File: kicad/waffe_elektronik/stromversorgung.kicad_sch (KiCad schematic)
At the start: 27 parts, among them Q3 FS8205A, U1 MT3608, U15 DW01A, U2 AMS1117-3.3, U3 MCP73831

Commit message: Platine: günstigere JLC-Teile, Option ESP32-S3-WROOM-1U mit externer Antenne
- Flash ZD35Q1GC-IB, Kondensatoren/Dioden/Widerstände auf Basic-Teile und 0402, Layout angepasst
- WROOM-1U auf demselben Footprint: eigene JLCPCB-BOM/CPL (Modulmitte 3,15 mm versetzt),
  Mouser-Option mit Pigtail RP-SMA/U.FL und Knick-Stabantenne, 3D-Modell des 1U
- Gerber, BOM, CPL, Renders und Bestelllisten neu erzeugt

Co-Authored-By: Claude Opus 5.5 <noreply@anthropic.com>
Claude-Session: https://claude.ai/code/session_01KkZzubjLKyW9odUwvmxTog
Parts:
- BT1: LCSC C225233 -> (none)
- C1: LCSC C723734 -> C23742
- C3: footprint Capacitor_Tantalum_SMD:CP_EIA-3528-21_Kemet-B -> Capacitor_Tantalum_SMD:CP_EIA-3216-18_Kemet-A; LCSC C7193 -> C7171
- D4: value SS14 -> B5819W; footprint Diode_SMD:D_SOD-123F -> Diode_SMD:D_SOD-123; LCSC C2909920 -> C8598
- D5: value BAT54WS -> 1N5819WS; LCSC C168799 -> C191023

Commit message: Fertigung: JLCPCB-BOM/CPL mit allen Steckern und Tastern (Variante komplett)
- Handlötteile tragen im Schaltplan das Feld "LCSC Hand" statt "LCSC", build_board.py übernimmt es
- jlc_fab.py schreibt zusätzlich *_komplett und *_komplett_externe_antenne (79 Teile, 20 Extended),
  --check prüft den Bedarf der Komplett-Variante; Rotationskorrektur 180° für JST-SH (ungeprüft)
- Schaltplan und Platine neu erzeugt (Geometrie unverändert), Gerber neu, Doku angepasst

Co-Authored-By: Claude Opus 5.5 <noreply@anthropic.com>
Claude-Session: https://claude.ai/code/session_01KkZzubjLKyW9odUwvmxTog
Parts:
- BT1: LCSC Hand (none) -> C225233

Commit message: Platine: microSD-Slot gedreht, Ein/Aus über den Drehgeber-Taster, R7 12 Ω, 10 µF am Slot
- J7: Karte wird auf der Kontaktseite eingesteckt (Datenblatt TF-018) -> Slot gedreht, Kontakte und
  Öffnung an der Unterkante, SD-Leitungen neu verlegt
- Soft-Power: Q4 (AO3401A) trennt den Akku von BAT_SW, Taster an J5.2 schaltet über D6 (BAT54CW) ein,
  IO21 hält über Q5, IO9 liest den Taster; Lasche oben links 18,6 x 9 mm mit den neuen Teilen,
  Leitungen auf B.Cu über die Oberkante, Akku-Plus über In2
- R7 12 Ω (C17913), C28 10 µF an der microSD-Versorgung
- Gerber, BOM/CPL (alle Varianten), Mouser-BOM, Renders und Doku neu

Co-Authored-By: Claude Opus 5.5 <noreply@anthropic.com>
Claude-Session: https://claude.ai/code/session_01KkZzubjLKyW9odUwvmxTog
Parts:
- added D6: BAT54CW, Package_TO_SOT_SMD:SOT-323_SC-70, symbol Diode:BAT54CW
- added Q4: AO3401A, Package_TO_SOT_SMD:SOT-23, symbol Transistor_FET:AO3401A
- added Q5: AO3400A, Package_TO_SOT_SMD:SOT-23, symbol Transistor_FET:AO3400A
- added R38, R40: 100k, Resistor_SMD:R_0603_1608Metric, symbol Device:R
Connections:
- net BAT_P: now also Q4.2 (S), R38.2; no longer C19.1, C5.1, L1.1, R3.1, U1.4 (EN), U1.5 (IN), U3.3 (V_{BAT})
- net GND: now also Q5.2 (S), R40.2
- new net: D6.1, Q4.1 (G), Q5.3 (D), R38.1
- new net BAT_SW: C19.1, C5.1, L1.1, Q4.3 (D), R3.1, U1.4 (EN), U1.5 (IN), U3.3 (V_{BAT})
- new net ENC_SW: D6.2
- new net PWR_HOLD: Q5.1 (G), R40.1
- new net PWR_KEY: D6.3
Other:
- note added: "Ein/Aus (Taster am Drehgeber)"
- note added: "Ein: Taster am Drehgeber drücken, ESP32 hält über IO21. Aus: IO21 low."
- note added: "Mit USB setzt die Firmware IO21 high: Laden über Q4."

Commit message: Platine: IP5306 (2 A Laden + 5 V) statt MT3608/MCP73831, Ein/Aus über KEY, eigener I²C-Bus
Co-Authored-By: Claude Opus 5.5 <noreply@anthropic.com>
Claude-Session: https://claude.ai/code/session_01KkZzubjLKyW9odUwvmxTog
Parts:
- removed D3: SS34, Diode_SMD:D_SMA, symbol Diode:SS34
- removed D5: 1N5819WS, Diode_SMD:D_SOD-323, symbol Device:D_Schottky
- removed Q4: AO3401A, Package_TO_SOT_SMD:SOT-23, symbol Transistor_FET:AO3401A
- removed Q5: AO3400A, Package_TO_SOT_SMD:SOT-23, symbol Transistor_FET:AO3400A
- removed R25: 10k, Resistor_SMD:R_0603_1608Metric, symbol Device:R
- removed U1: MT3608, Package_TO_SOT_SMD:SOT-23-6, symbol Regulator_Switching:MT3608
- removed U3: MCP73831, Package_TO_SOT_SMD:SOT-23-5, symbol Battery_Management:MCP73831-2-OT
- added C29: 10u, Capacitor_SMD:C_0603_1608Metric, symbol Device:C
- added C30: 22u, Capacitor_SMD:C_0805_2012Metric, symbol Device:C
- added U1: IP5306-I2C, Package_SO:HSOP-8-1EP_3.9x4.9mm_P1.27mm_EP2.3x2.3mm_ThermalVias, symbol lasertag:IP5306
- C4: value 1u -> 10u; footprint Capacitor_SMD:C_0603_1608Metric -> Capacitor_SMD:C_0805_2012Metric; LCSC C15849 -> C15850
- C5: value 1u -> 22u; LCSC C15849 -> C59461
- L1: value 10u -> 1u; LCSC C408412 -> C408355
- R1: value 2k -> 2; LCSC C22975 -> C22977
- R2: value 10k -> 1; LCSC C25804 -> C22936
- R24: value 75k -> 10k; LCSC C23242 -> C25804
- R3, R4: value 100k -> 1M; LCSC C25803 -> C22935
- R38, R40: value 100k -> 4.7k; footprint Resistor_SMD:R_0603_1608Metric -> Resistor_SMD:R_0402_1005Metric; LCSC C25803 -> C25900
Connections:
- net CHRG_STAT is gone; now on net BAT_P: R2.2
- net PWR_HOLD is gone; now on net 3V3_MCU: R40.1
- net 3V3_MCU: now also R38.1; no longer R2.1
- net 5V_PERIPH: now also C30.1, U1.8 (VOUT); no longer R24.1
- net BAT_P: now also C19.1, L1.2, R3.1; no longer R38.2
- net GND: now also C29.2, C30.2, U1.9 (GND); no longer R1.2, R40.2
- net VBUS_NATIVE: now also R1.1, U1.1 (VIN)
- net at D6.1: now also R24.2; no longer R38.1
- removed net BAT_SW: C19.1, C5.1, L1.1, R3.1
- new net: C29.1, R1.2
- new net: C5.1, R2.1, U1.6 (BAT)
- new net: L1.1, U1.7 (SW)
- new net IP_KEY: R24.1, U1.5 (KEY)
- new net IP_SCL: R40.2, U1.2 (SCL)
- new net IP_SDA: R38.2, U1.3 (SDA)
- no-connect marks 1 -> 2
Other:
- note added: "Akku + Ein/Aus (Taster am Drehgeber)"
- note added: "Ein: Taster am Drehgeber kurz drücken. Aus: 2 s drücken oder per I²C (Firmware)."
- note added: "Laden + 5 V (IP5306) + 3,3 V"
- note added: "Laden 2 A (USB-C), 5 V Boost, Ein/Aus-Taste; Register per I²C (Firmware)"
- note removed: "Ein/Aus (Taster am Drehgeber)"
- note removed: "Ein: Taster am Drehgeber drücken, ESP32 hält über IO21. Aus: IO21 low."
- note removed: "Laden (USB-C)"
- note removed: "Mit USB setzt die Firmware IO21 high: Laden über Q4."
- note removed: "Stromversorgung"

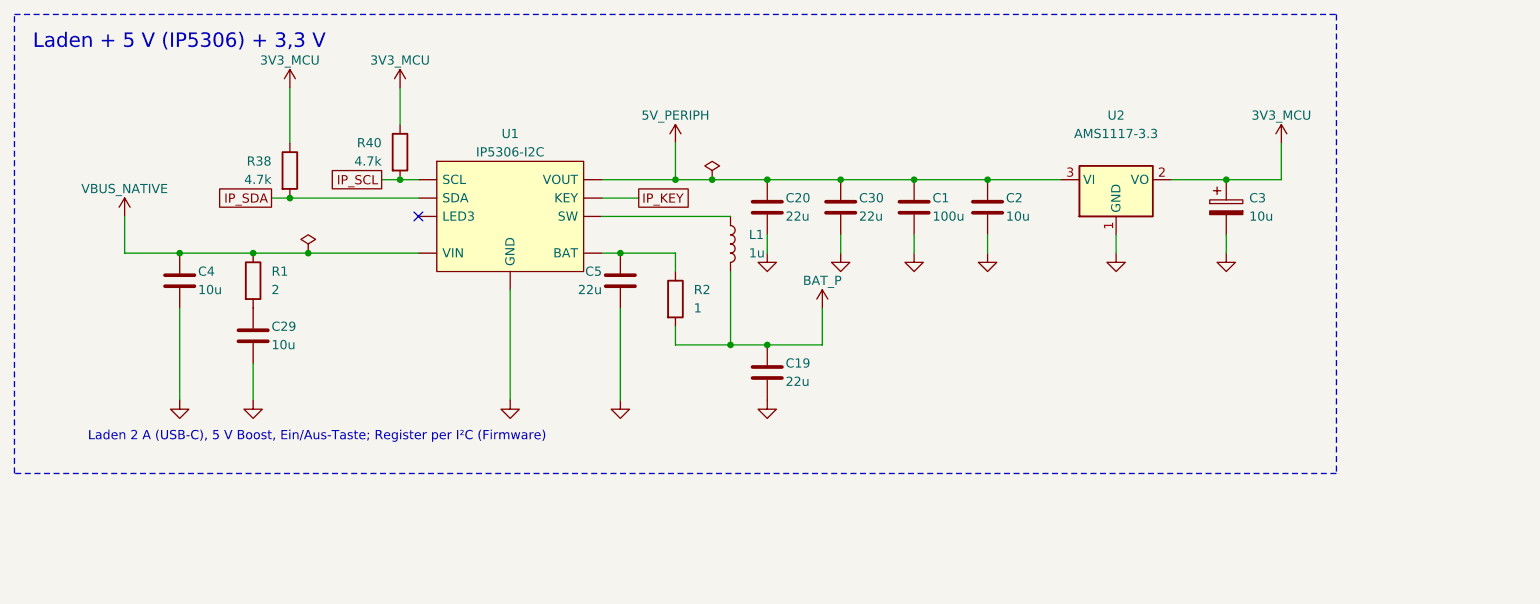
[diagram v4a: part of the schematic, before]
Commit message: Platine: Stecker zusammengelegt, Basic-Teile, MOSFET-Pegelwandler, Flash optional, Kabel-3V3 über 10 Ω, breitere 5-V- und Akku-Wege
Co-Authored-By: Claude Opus 5.5 <noreply@anthropic.com>
Claude-Session: https://claude.ai/code/session_01KkZzubjLKyW9odUwvmxTog
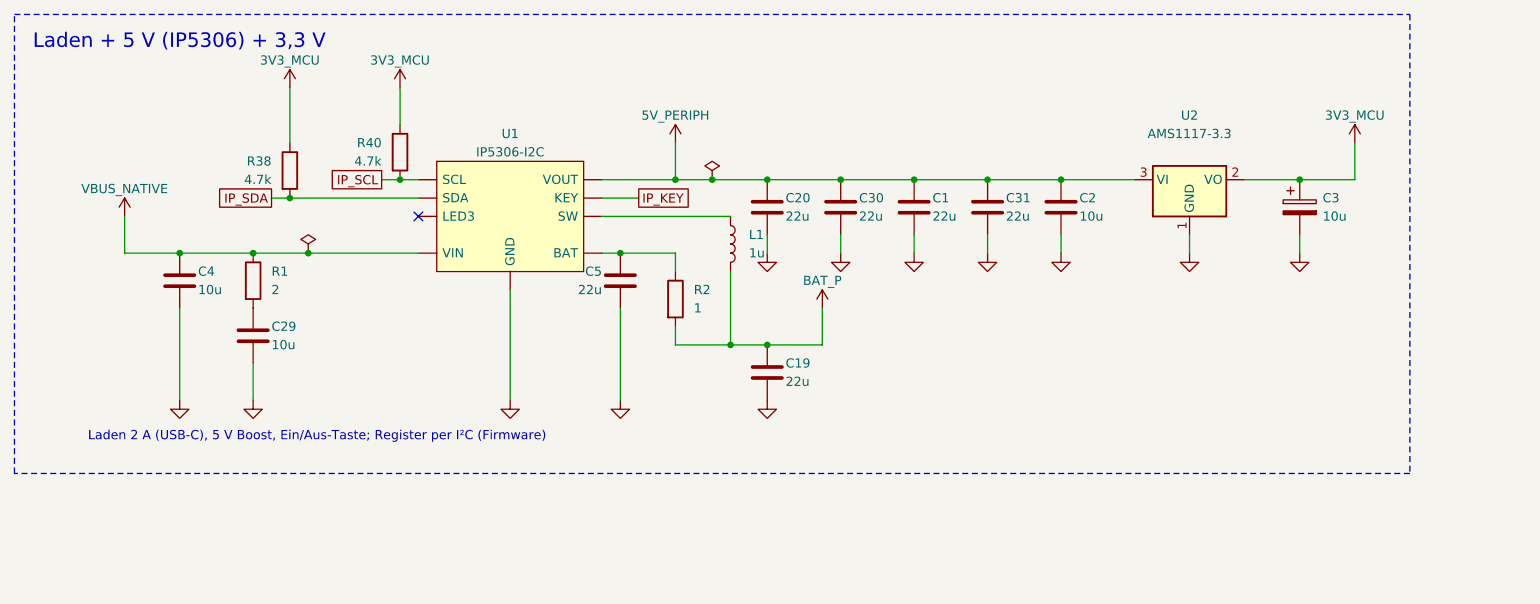
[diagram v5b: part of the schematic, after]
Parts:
- added C31: 22u, Capacitor_SMD:C_0805_2012Metric, symbol Device:C
- C1: value 100u -> 22u; footprint Capacitor_SMD:C_1210_3225Metric -> Capacitor_SMD:C_0805_2012Metric; LCSC C23742 -> C45783
- D6: LCSC C83573 -> C57891
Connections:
- net 5V_PERIPH: now also C31.1
- net GND: now also C31.2

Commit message: Platine: Lastschalter TPS22810 hinter dem IP5306 (EN = IRQ), RESET in die Lasche, Dämpfung an der USB-Buchse
Co-Authored-By: Claude Opus 5.5 <noreply@anthropic.com>
Claude-Session: https://claude.ai/code/session_01KkZzubjLKyW9odUwvmxTog
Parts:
- added C33: 10n, Capacitor_SMD:C_0402_1005Metric, symbol Device:C
- added R42: 100k, Resistor_SMD:R_0603_1608Metric, symbol Device:R
- added U16: TPS22810, Package_TO_SOT_SMD:SOT-23-6, symbol Power_Management:TPS22810DBV
- C30: value 22u -> 10u; footprint Capacitor_SMD:C_0805_2012Metric -> Capacitor_SMD:C_0603_1608Metric; LCSC C45783 -> C19702
- C4: footprint Capacitor_SMD:C_0805_2012Metric -> Capacitor_SMD:C_0603_1608Metric; LCSC C15850 -> C19702
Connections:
- net 5V_PERIPH: now also U16.6 (VOUT); no longer C20.1, C30.1, U1.8 (VOUT)
- net GND: now also C33.2, R42.2, U16.2 (GND)
- net IP_IRQ: now reaches U1.4 (IRQ)
- net IP_IRQ: now also R42.1, U16.3 (EN/UVLO)
- new net: C20.1, C30.1, U1.8 (VOUT), U16.1 (VIN)
- new net: C33.1, U16.4 (CT)
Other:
- note added: "Laden + 5 V (IP5306, Lastschalter) + 3,3 V"
- note removed: "Laden + 5 V (IP5306) + 3,3 V"
